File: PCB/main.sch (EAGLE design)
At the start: 51 parts, among them J1 DC-005, Q1 CSD17578Q3A

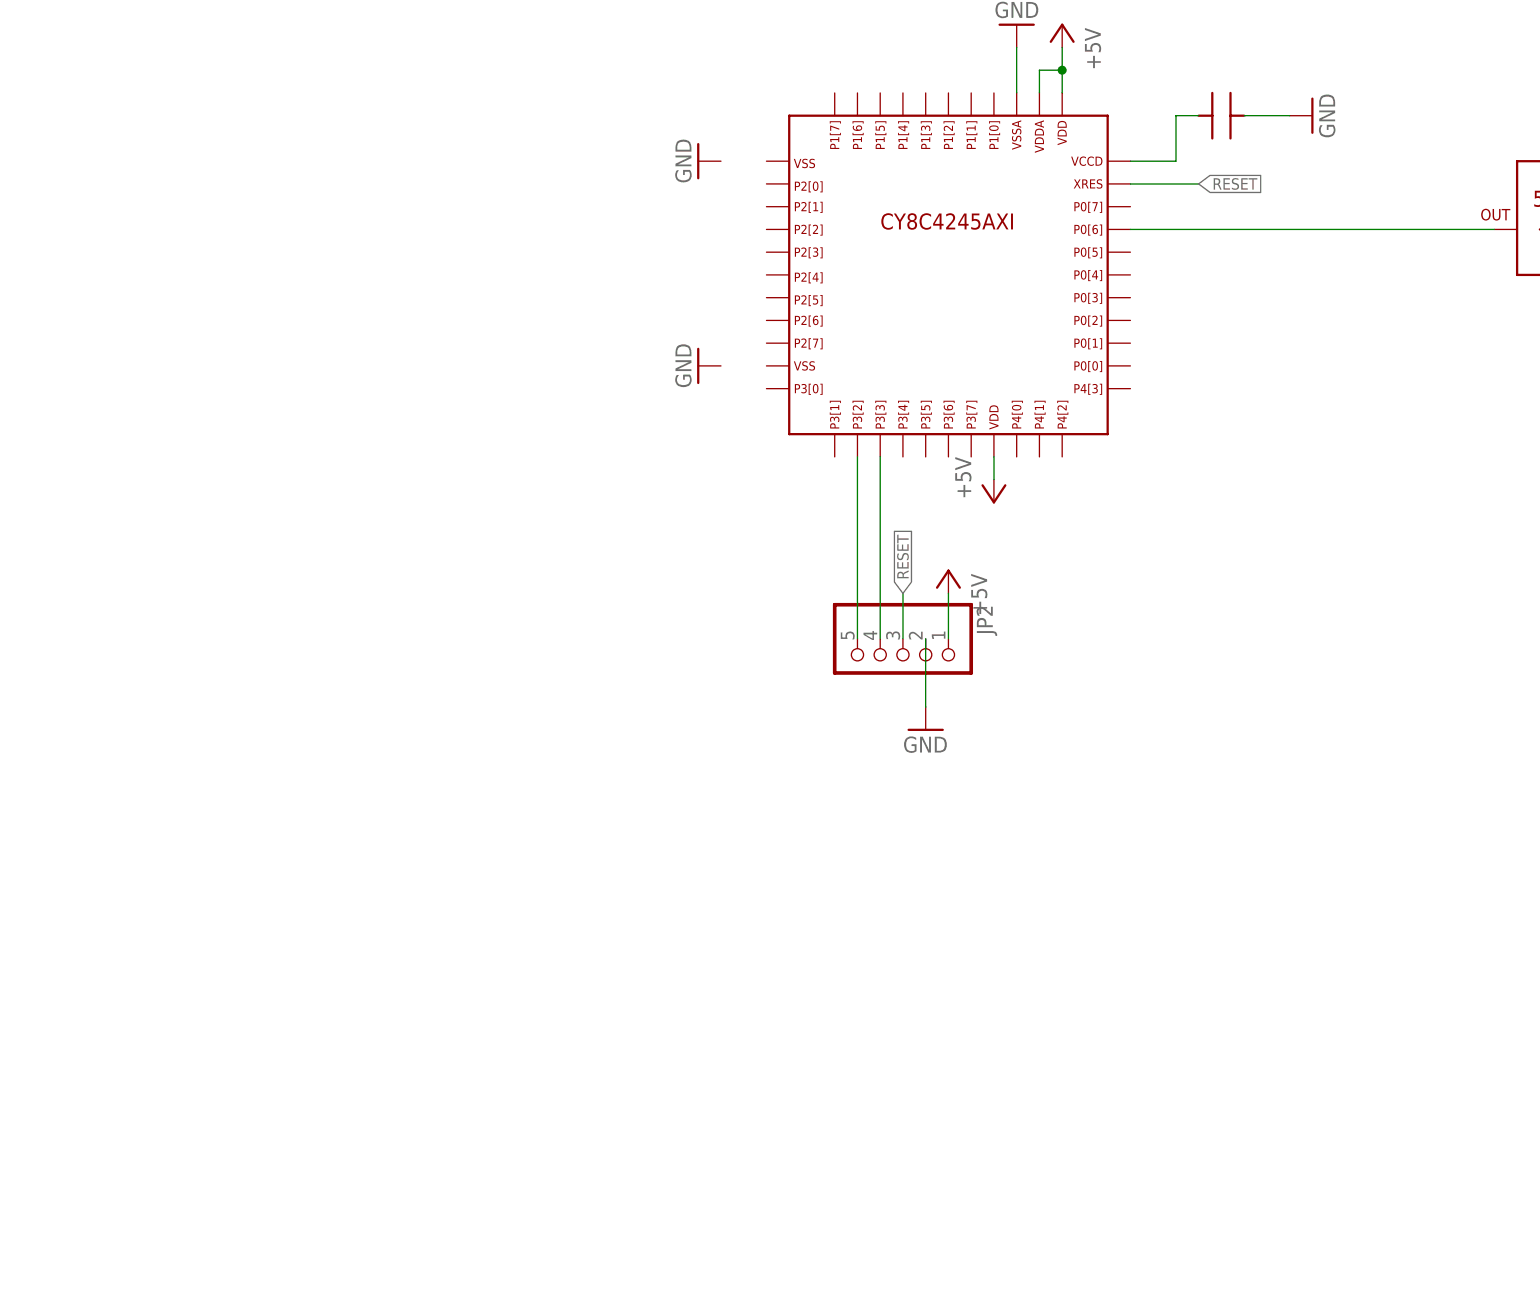
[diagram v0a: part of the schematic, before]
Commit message: Create PSoC project
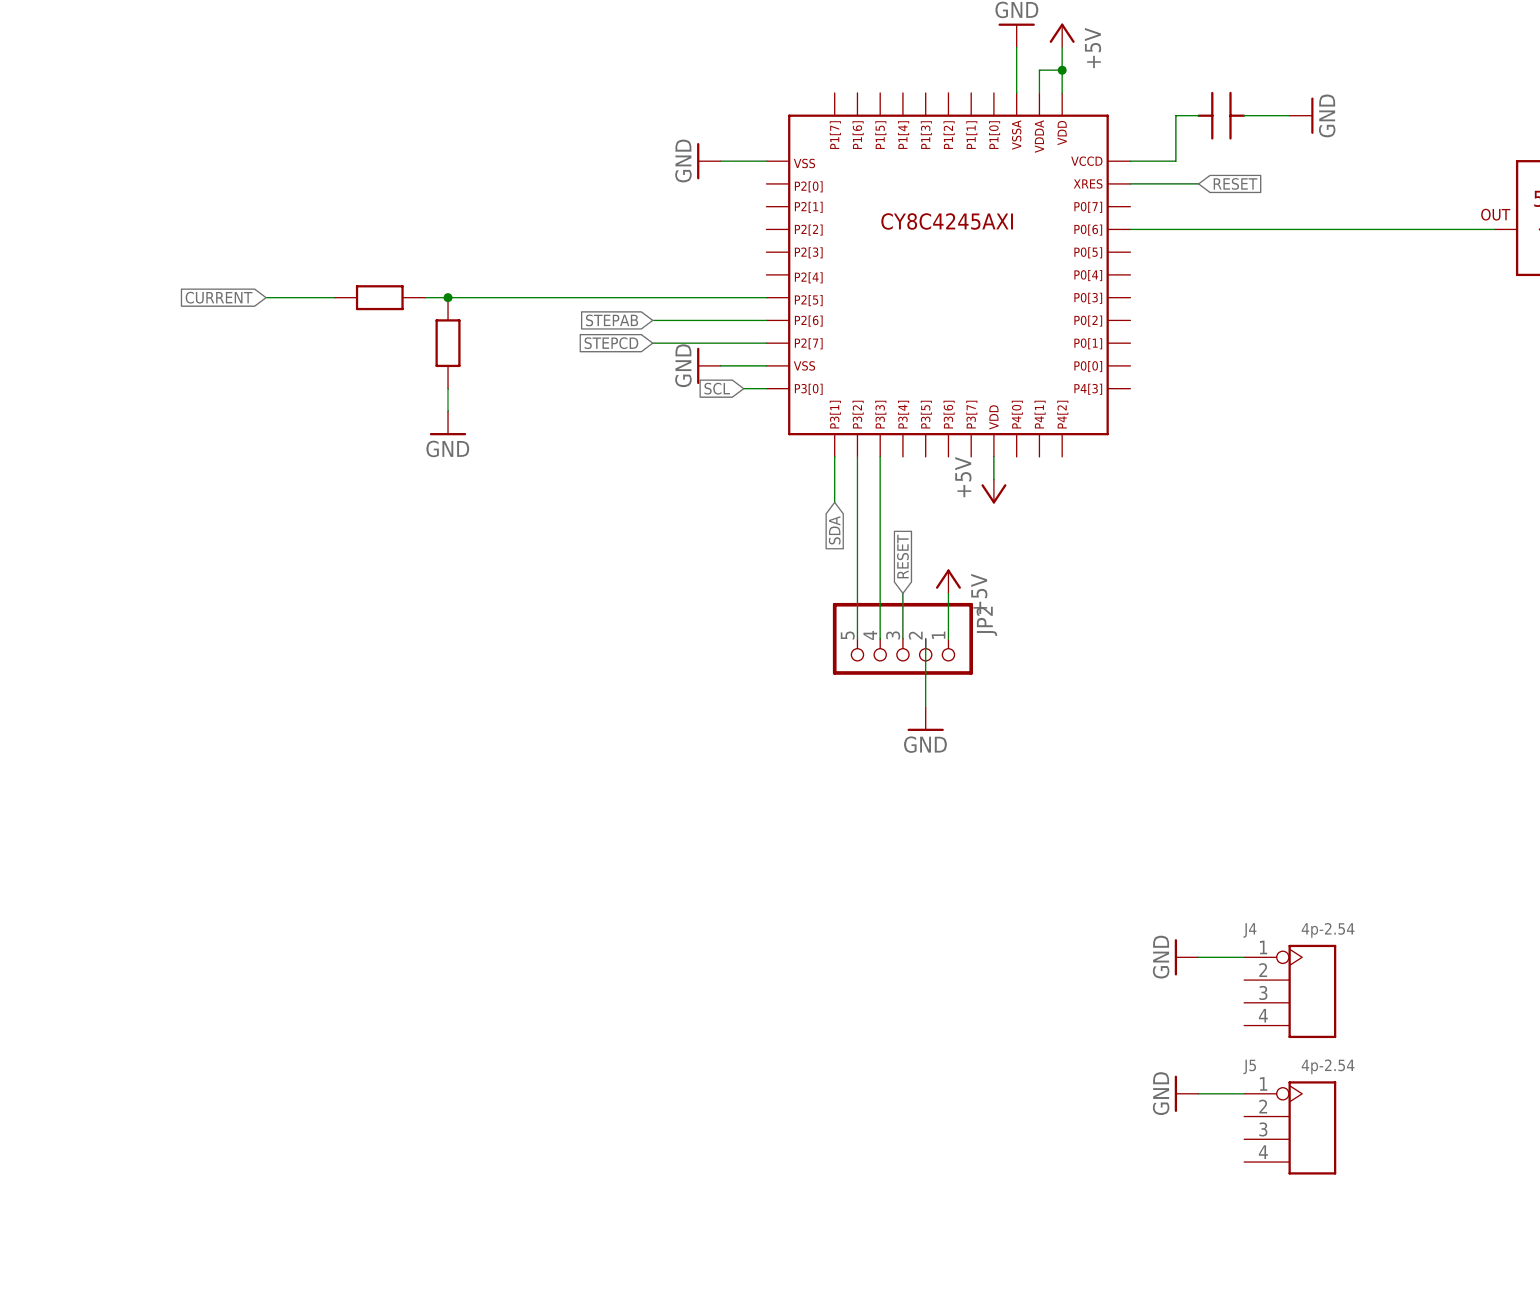
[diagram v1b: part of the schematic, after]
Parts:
- added J4, J5: 4p-2.54, Seeed-OPL-Connector:DIP-BLACK-FEMALE-HEADER-VERT(4P-2.54)
- added R17, R18: (no value), My_RLC:RES0603
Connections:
- new net N$60: R17.P$2, R18.P$1, U$1.7
- net CURRENT: now also R18.P$2
- net GND: now also J4.P$1, J5.P$1, R17.P$1, U$1.1, U$1.10
- net SCL: now also U$1.11
- net SDA: now also U$1.12
- net STEPAB: now also U$1.8
- net STEPCD: now also U$1.9
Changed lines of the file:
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@@
 <?xml version="1.0" encoding="utf-8"?>
 <!DOCTYPE eagle SYSTEM "eagle.dtd">
-<eagle version="6.5.0">
+<eagle version="7.1.0">
 <drawing>
 <settings>
@@
 <part name="C14" library="My_RLC" deviceset="CAP0603" device=""/>
 <part name="P+20" library="supply1" deviceset="+5V" device=""/>
+<part name="J4" library="Seeed-OPL-Connector" deviceset="DIP-BLACK-FEMALE-HEADER-VERT(4P-2.54)" device="" value="4p-2.54"/>
+<part name="J5" library="Seeed-OPL-Connector" deviceset="DIP-BLACK-FEMALE-HEADER-VERT(4P-2.54)" device="" value="4p-2.54"/>
+<part name="GND23" library="supply1" deviceset="GND" device=""/>
+<part name="GND24" library="supply1" deviceset="GND" device=""/>
+<part name="R17" library="My_RLC" deviceset="RES0603" device=""/>
+<part name="R18" library="My_RLC" deviceset="RES0603" device=""/>
+<part name="GND25" library="supply1" deviceset="GND" device=""/>
 </parts>
 <sheets>
@@
 <instance part="C14" gate="G$1" x="269.24" y="177.8" rot="R270"/>
 <instance part="P+20" gate="1" x="261.62" y="101.6" rot="MR180"/>
+<instance part="J4" gate="G$1" x="297.18" y="46.99"/>
+<instance part="J5" gate="G$1" x="297.18" y="31.75"/>
+<instance part="GND23" gate="1" x="281.94" y="50.8" rot="R270"/>
+<instance part="GND24" gate="1" x="281.94" y="35.56" rot="R270"/>
+<instance part="R17" gate="G$1" x="200.66" y="119.38" rot="R90"/>
+<instance part="R18" gate="G$1" x="193.04" y="124.46" rot="R180"/>
+<instance part="GND25" gate="1" x="200.66" y="109.22"/>
 </instances>
 <busses>
@@
 <label x="20.32" y="149.86" size="1.27" layer="95" xref="yes"/>
 </segment>
+<segment>
+<wire x1="180.34" y1="124.46" x2="187.96" y2="124.46" width="0.1524" layer="91"/>
+<label x="180.34" y="124.46" size="1.27" layer="95" rot="R180" xref="yes"/>
+<pinref part="R18" gate="G$1" pin="P$2"/>
+</segment>
 </net>
 <net name="N$19" class="0">
@@
 <pinref part="R16" gate="G$1" pin="P$1"/>
 </segment>
+<segment>
+<wire x1="243.84" y1="106.68" x2="243.84" y2="101.6" width="0.1524" layer="91"/>
+<label x="243.84" y="101.6" size="1.27" layer="95" rot="MR270" xref="yes"/>
+<pinref part="U$1" gate="G$1" pin="12"/>
+</segment>
 </net>
 <net name="SCL" class="0">
@@
 <pinref part="R15" gate="G$1" pin="P$1"/>
 </segment>
+<segment>
+<wire x1="236.22" y1="114.3" x2="233.68" y2="114.3" width="0.1524" layer="91"/>
+<label x="233.68" y="114.3" size="1.27" layer="95" rot="MR0" xref="yes"/>
+<pinref part="U$1" gate="G$1" pin="11"/>
+</segment>
 </net>
 <net name="STEPAB" class="0">
@@
 <label x="-40.64" y="20.32" size="1.27" layer="95" xref="yes"/>
 </segment>
+<segment>
+<label x="223.52" y="121.92" size="1.27" layer="95" rot="R180" xref="yes"/>
+<pinref part="U$1" gate="G$1" pin="8"/>
+<wire x1="223.52" y1="121.92" x2="236.22" y2="121.92" width="0.1524" layer="91"/>
+</segment>
 </net>
 <net name="STEPCD" class="0">
@@
 <pinref part="J3" gate="G$1" pin="2"/>
 <label x="-40.64" y="25.4" size="1.27" layer="95" xref="yes"/>
+</segment>
+<segment>
+<label x="223.52" y="119.38" size="1.27" layer="95" rot="R180" xref="yes"/>
+<pinref part="U$1" gate="G$1" pin="9"/>
+<wire x1="236.22" y1="119.38" x2="223.52" y2="119.38" width="0.1524" layer="91"/>
 </segment>
 </net>
@@
 <junction x="264.16" y="175.26"/>
 </segment>
+<segment>
+<pinref part="U$1" gate="G$1" pin="10"/>
+<pinref part="GND17" gate="1" pin="GND"/>
+<wire x1="236.22" y1="116.84" x2="231.14" y2="116.84" width="0.1524" layer="91"/>
+</segment>
+<segment>
+<pinref part="U$1" gate="G$1" pin="1"/>
+<pinref part="GND18" gate="1" pin="GND"/>
+<wire x1="236.22" y1="139.7" x2="231.14" y2="139.7" width="0.1524" layer="91"/>
+</segment>
+<segment>
+<pinref part="J4" gate="G$1" pin="P$1"/>
+<pinref part="GND23" gate="1" pin="GND"/>
+<wire x1="289.56" y1="50.8" x2="284.48" y2="50.8" width="0.1524" layer="91"/>
+</segment>
+<segment>
+<pinref part="J5" gate="G$1" pin="P$1"/>
+<pinref part="GND24" gate="1" pin="GND"/>
+<wire x1="289.56" y1="35.56" x2="284.48" y2="35.56" width="0.1524" layer="91"/>
+</segment>
+<segment>
+<pinref part="R17" gate="G$1" pin="P$1"/>
+<pinref part="GND25" gate="1" pin="GND"/>
+<wire x1="200.66" y1="114.3" x2="200.66" y2="111.76" width="0.1524" layer="91"/>
+</segment>
 </net>
 <net name="N$58" class="0">
@@
 </segment>
 </net>
+<net name="N$60" class="0">
+<segment>
+<pinref part="R17" gate="G$1" pin="P$2"/>
+<pinref part="R18" gate="G$1" pin="P$1"/>
+<wire x1="200.66" y1="124.46" x2="198.12" y2="124.46" width="0.1524" layer="91"/>
+<pinref part="U$1" gate="G$1" pin="7"/>
+<wire x1="200.66" y1="124.46" x2="236.22" y2="124.46" width="0.1524" layer="91"/>
+<junction x="200.66" y="124.46"/>
+</segment>
+</net>

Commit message: Reroute PCB
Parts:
- removed C10, C8, C9: (no value), My_RLC:CAP0603
- removed J3: (no value), Seeed-OPL-Connector:DIP-BLACK-FEMALE-HEADER-VERT(2P-2.54)
- removed J5: 4p-2.54, Seeed-OPL-Connector:DIP-BLACK-FEMALE-HEADER-VERT(4P-2.54)
- removed R14, R15, R16, R17, R18: (no value), My_RLC:RES0603
- removed U$2: MCP23017T-E/ML, I2C:MCP23017T-E/ML
- removed U$3: MYB, Button:MYB
- added S1, S2, S3, S4: (no value), switch-omron:10-XX
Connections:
- removed net N$44: R13.P$2, U$2.P$4
- removed net N$45: R12.P$2, U$2.P$3
- removed net N$46: R11.P$2, U$2.P$2
- removed net N$47: R10.P$2, U$2.P$24
- removed net N$48: R9.P$2, U$2.P$23
- removed net N$49: R8.P$2, U$2.P$22
- removed net N$50: C8.P$2, R14.P$1, U$2.P$14, U$3.1
- removed net N$60: R17.P$2, R18.P$1, U$1.7
- removed net SCL: R15.P$1, U$1.11, U$2.P$8
- removed net SDA: R16.P$1, U$1.12, U$2.P$9
- removed net STEPAB: DRV1.ABSTEP, J3.1, U$1.8
- removed net STEPCD: DRV1.CDSTEP, J3.2, U$1.9
- new net ABDIR: DRV1.ABDIR, U$1.41
- new net ABENBLN: DRV1.ABENBLN, U$1.42
- new net ABRESETN: DRV1.ABRESETN, U$1.44
- new net ABSTEP: DRV1.ABSTEP, U$1.39
- new net ABUSM0: DRV1.ABUSM0, U$1.40
- new net ABUSM1: DRV1.ABUSM1, U$1.43
- new net CDDIR: DRV1.CDDIR, U$1.4
- new net CDENBLN: DRV1.CDENBLN, U$1.5
- new net CDRESETN: DRV1.CDRESETN, U$1.7
- new net CDSTEP: DRV1.CDSTEP, U$1.2
- new net CDUSM0: DRV1.CDUSM0, U$1.3
- new net CDUSM1: DRV1.CDUSM1, U$1.6
- net +24V: no longer C4.1, I_IC1.P$10
- net +3V3: now also C4.1, I_IC1.P$10
- net +5V: no longer C10.P$2, C9.P$2, R14.P$2, R15.P$2, R16.P$2, U$2.P$5
- net CURRENT: now also U$1.8; no longer R18.P$2
- net GND: now also LED2.C, LED3.C, LED4.C, LED5.C, LED6.C, LED7.C, S1.S, S1.S1, S2.S, S2.S1, S3.S, S3.S1, S4.S, S4.S1; no longer J5.P$1, R17.P$1
- net GNDA: no longer C10.P$1, C8.P$1, C9.P$1, LED2.C, LED3.C, LED4.C, LED5.C, LED6.C, LED7.C, U$2.P$11, U$2.P$12, U$2.P$13, U$2.P$6, U$3.2
- net N$28: now also R13.P$2, U$1.28; no longer DRV1.ABUSM0, U$2.P$17
- net N$29: now also R12.P$2, U$1.27; no longer DRV1.ABDIR, U$2.P$18
- net N$30: now also R11.P$2, U$1.26; no longer DRV1.ABENBLN, U$2.P$19
- net N$31: now also R10.P$2, U$1.25; no longer DRV1.ABUSM1, U$2.P$20
- net N$32: now also R9.P$2, U$1.24; no longer DRV1.ABRESETN, U$2.P$21
- net N$33: now also R8.P$2, U$1.23; no longer DRV1.CDUSM0, U$2.P$25
- net N$34: now also S1.P, U$1.38; no longer DRV1.CDDIR, U$2.P$26
- net N$35: now also S2.P, U$1.37; no longer DRV1.CDENBLN, U$2.P$27
- net N$36: now also S3.P, U$1.31; no longer DRV1.CDUSM1, U$2.P$28
- net N$37: now also S4.P1, U$1.29; no longer DRV1.CDRESETN, U$2.P$1
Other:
- moved on the sheet: JP2, LDO2, LED2, LED3, LED4, LED5, LED6, LED7

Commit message: Bug Fix/ Final Version
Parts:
- added LED8, LED9: (no value), led:LEDCHIP-LED0603
- added R14, R15, R17: (no value), My_RLC:RES0603
- added R16: (no value), rcl:R-EU_M0805
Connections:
- new net N$44: J4.P$2, LED8.C, U$1.12
- new net N$45: J4.P$3, LED9.C, U$1.11
- new net N$48: R17.P$2, U$4.EN
- new net N$49: LED9.A, R15.P$1
- new net N$50: LED8.A, R14.P$1
- net +3V3: now also R17.P$1; no longer C4.1, I_IC1.P$10, U$4.EN
- net +5V: now also C4.1, I_IC1.P$10, J4.P$4, R14.P$2, R15.P$2
- net AGND: now also Q1.D; no longer Q1.S
- net GND: now also R16.2
- net GNDA: now also R16.1
- net N$1: now also Q1.S; no longer Q1.D
- net N$34: now also S1.P1
- net N$35: now also S2.P1
- net N$36: now also S3.P1
- net N$37: now also S4.P
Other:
- moved on the sheet: Q1

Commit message: Change Power Regulator
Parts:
- removed J2: (no value), Seeed-OPL-Connector:DIP-BLACK-FEMALE-HEADER-VERT(2P-2.54)
- removed LDO1: TPS7A470X, My_TI:TPS7A470X
- removed LDO2: TPS736, My_TI:TPS736
- removed LED7: (no value), led:LEDCHIP-LED0603
- added C10, C8, C9: (no value), My_RLC:CAP0603
- added D1: (no value), diode:DIODE-DO-214AC
- added D2: (no value), diode:DIODE_2CACA-SOT23
- added DC/DC1: (no value), My_TI:LM25011
- added JP3: (no value), pinhead:PINHD-2X3
- added L1: (no value), My_RLC:L0603
- added R18, R19, R20, R21: (no value), My_RLC:RES0603
- C1: device rcl:CPOL-EU150CLZ-1010 -> rcl:CPOL-EUSMCD
- C2: device rcl:C-EUC0805 -> My_RLC:CAP0603
- R3: device rcl:R-EU_M0805 -> My_RLC:RES0603
- R8: device My_RLC:RES0603 -> rcl:R-EU_M0805
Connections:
- removed net +5V: C12.P$1, C3.+, C4.1, I_IC1.P$10, J2.2, J4.P$4, JP2.1, LDO1.OUT, LDO1.OUT@1, LDO1.SENSE, LDO2.EN, LDO2.IN, R14.P$2, R15.P$2, U$1.19, U$1.34, U$1.35
- removed net N$34: S1.P, S1.P1, U$1.38
- removed net N$35: S2.P, S2.P1, U$1.37
- new net ABDECACY: DRV1.ABDECAY, U$1.38
- new net BUT1: S1.P, S1.P1, U$1.15
- new net BUT2: S2.P, S2.P1, U$1.17
- new net CDDECACY: DRV1.CDDECAY, U$1.2
- new net N$20: JP3.4, U$1.23
- new net N$26: DC/DC1.2, R18.P$1
- new net N$5: C8.P$2, DC/DC1.4
- new net N$51: C9.P$2, DC/DC1.10
- new net N$52: C9.P$1, D2.C, DC/DC1.9, L1.P$1
- new net N$60: DC/DC1.6, R20.P$1, R21.P$2
- new net VCC: C6.2, DRV1.VM, DRV1.VM@1, DRV1.VM@2, DRV1.VM@3, I_IC1.P$1, I_IC1.P$2, I_IC1.P$3
- net +24V: now also D1.A, I_IC1.P$14, I_IC1.P$15, I_IC1.P$16, R3.P$2; no longer C6.2, DRV1.VM, DRV1.VM@1, DRV1.VM@2, DRV1.VM@3, LDO1.EN, LDO1.IN, LDO1.IN@1, R3.2
- net +3V3: now also C10.P$1, C12.P$1, C13.P$1, C3.+, C4.1, I_IC1.P$10, J4.P$4, JP2.1, JP3.1, L1.P$2, R14.P$2, R15.P$2, R21.P$1, U$1.19, U$1.34, U$1.35; no longer LDO2.OUT
- net AGND: now also C14.P$2, C2.P$1, C8.P$1, DC/DC1.5, DC/DC1.7, R16.1, R19.P$1, R20.P$2, R8.1; no longer C2.1, I_IC1.P$1, I_IC1.P$2, I_IC1.P$3, I_IC1.P$6, LDO1.0P1V, LDO1.0P2V, LDO1.1P6V, LDO1.3P2V, LDO1.EPAD, LDO1.GND, LDO1.NC
- net CDDIR: now also U$1.5; no longer U$1.4
- net CDENBLN: now also U$1.6; no longer U$1.5
- net CDRESETN: now also U$1.8; no longer U$1.7
- net CDSTEP: now also U$1.3; no longer U$1.2
- net CDUSM0: now also U$1.4; no longer U$1.3
- net CDUSM1: now also U$1.7; no longer U$1.6
- net CURRENT: now also U$1.9; no longer U$1.8
- net GND: now also C10.P$2, JP3.2; no longer C14.P$2, LDO2.GND, LED7.C
- net GNDA: now also R8.2; no longer I_IC1.P$14, I_IC1.P$15, I_IC1.P$16, R16.1
- net N$2: now also C2.P$2, D1.C, DC/DC1.1, R18.P$2; no longer C2.2, LDO1.NR
- net N$25: now also JP3.3, U$1.22; no longer C7.1, DRV1.V3P3
- net N$27: now also C7.1, DRV1.V3P3; no longer J2.1
- net N$33: now also JP3.5, U$1.21; no longer R8.P$2, U$1.23
- net N$38: now also JP3.6, U$1.20; no longer LED7.A, R8.P$1
- net N$4: now also R3.P$1; no longer R3.1
- net N$57: now also D2.AC, DC/DC1.8, R19.P$2; no longer C13.P$1, LDO2.NR
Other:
- moved on the sheet: C3, R16
